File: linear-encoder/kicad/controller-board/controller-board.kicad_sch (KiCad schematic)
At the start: 22 parts, among them J1 RJ45 X - NO MAGNETICS, J2 RJ45 Y - NO MAGNETICS, J3 RJ45 A - NO MAGNETICS, J4 RJ45 Z - NO MAGNETICS, J5 P1 2.00mm 2x10

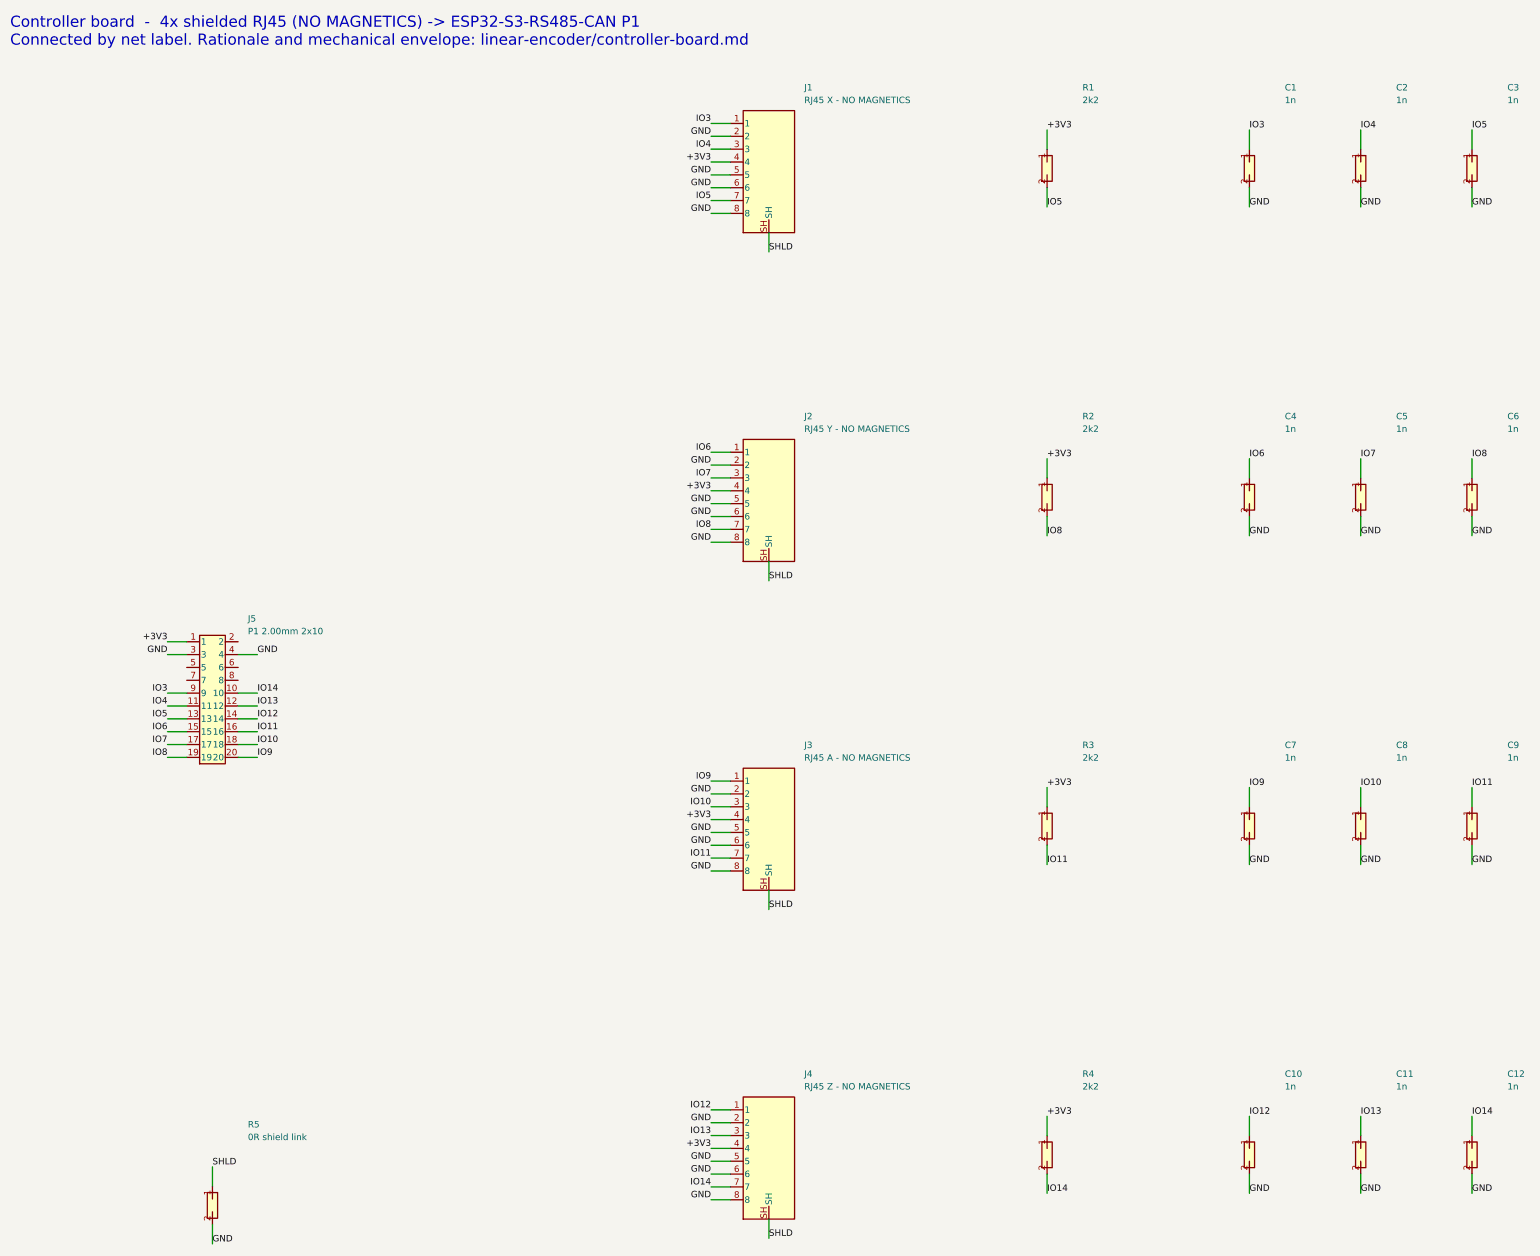
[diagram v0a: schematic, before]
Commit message: The schematic is verified now, not merely written
KiCad 10.0.5 installed, so the previous commit's "nobody has opened it" caveat is
discharged with evidence rather than removed:

  - kicad-cli sch erc and sch export netlist both load the file.
  - KiCad's OWN extracted netlist matches netlist.txt exactly - all 15 nets, zero
    mismatches, no extra or missing nodes. That is the check that matters: it proves
    the net labels actually attached to the pins rather than merely sitting near them.

ERC went 134 -> 22. The 112 fixed were real:

  - 107 endpoint_off_grid. Placement origins were not multiples of 1.27mm, so every
    pin and stub sat off the connection grid. Connections resolved anyway, which is
    exactly what makes it worth fixing - off-grid endpoints can silently fail to
    connect once a human edits the sheet. generate.py now snaps origins.
  - 5 pin_not_connected: header pins 2 (5V), 5/7 (UART), 6/8 (USB), deliberately
    unused. no_connect markers turn an error into a recorded decision.

The 22 remaining are all lib_symbol_issues - the symbols are embedded rather than
from a configured library. Left alone deliberately: the warning is true, and those
symbols ARE placeholders that must be swapped for real parts before layout.

generate.py is now in the repo. It produced the schematic, the project file and the
netlist from one source, which is why the netlist and the drawing cannot disagree -
and it is the thing to edit until the board is opened for real layout work.

Co-Authored-By: Claude Opus 5 <noreply@anthropic.com>
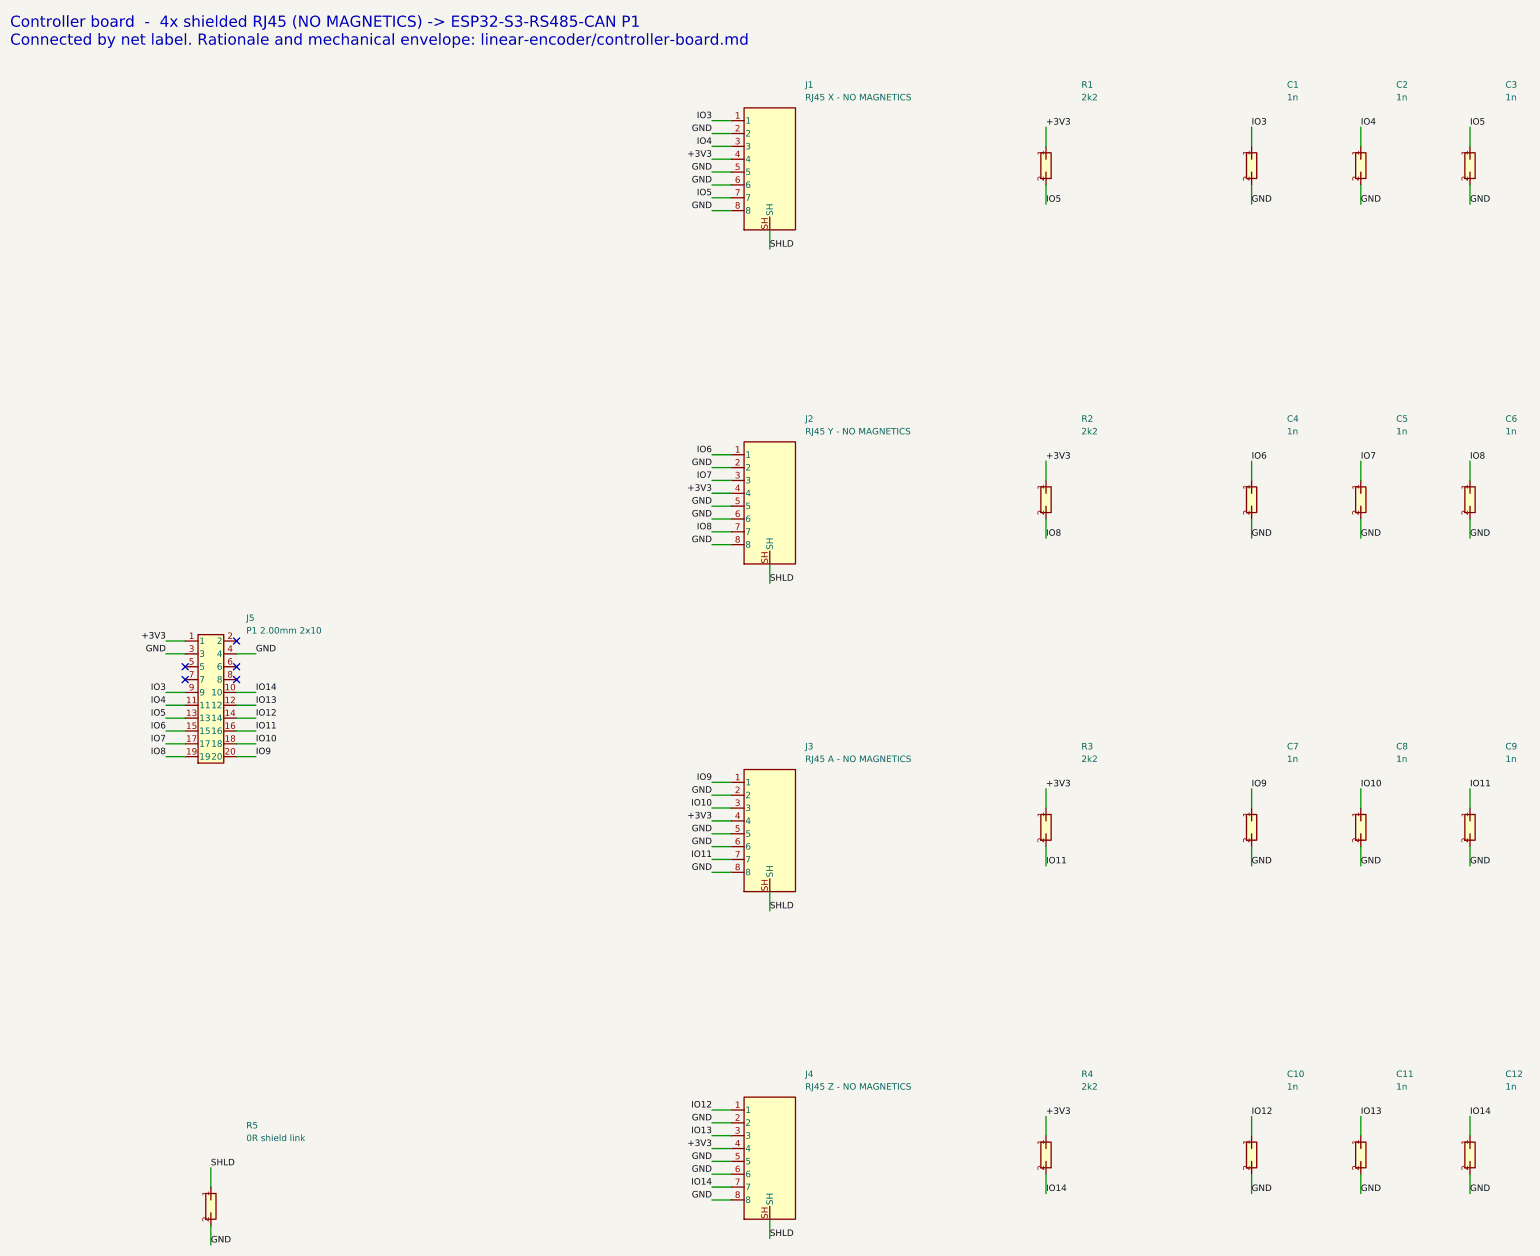
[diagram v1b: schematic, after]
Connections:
- no-connect marks 0 -> 5
